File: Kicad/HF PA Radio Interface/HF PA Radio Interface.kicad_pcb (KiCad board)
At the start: 2 copper layers, 100 x 100 mm, 187 parts, among them J1 Conn_01x06, J10 Conn_01x03, J11 Conn_01x04, J12 Conn_01x02, J13 Conn_01x02, J14 Conn_01x02, J15 Conn_01x03, J16 Conn_01x04, J17 Conn_01x04, J18 Conn_01x04, J2 Conn_Coaxial, J3 Conn_Coaxial, J4 Conn_Coaxial, J5 Conn_01x05, J6 Conn_01x05, J7 Conn_01x04, J8 Conn_01x04, J9 Conn_01x04, K1 G2RL-1-E, Q1 BC848W, Q2 2N7002, Q3 DMG2305UX, U1 74LVC1G17, U10 74AHCT125, U2 74LVC74, U3 TLV9364, U4 ADS1015IDGS, U5 TLV9361, U6 MCP4728, U7 AP2204K-ADJ, U8 LTC1044, U9 74LVC1G17

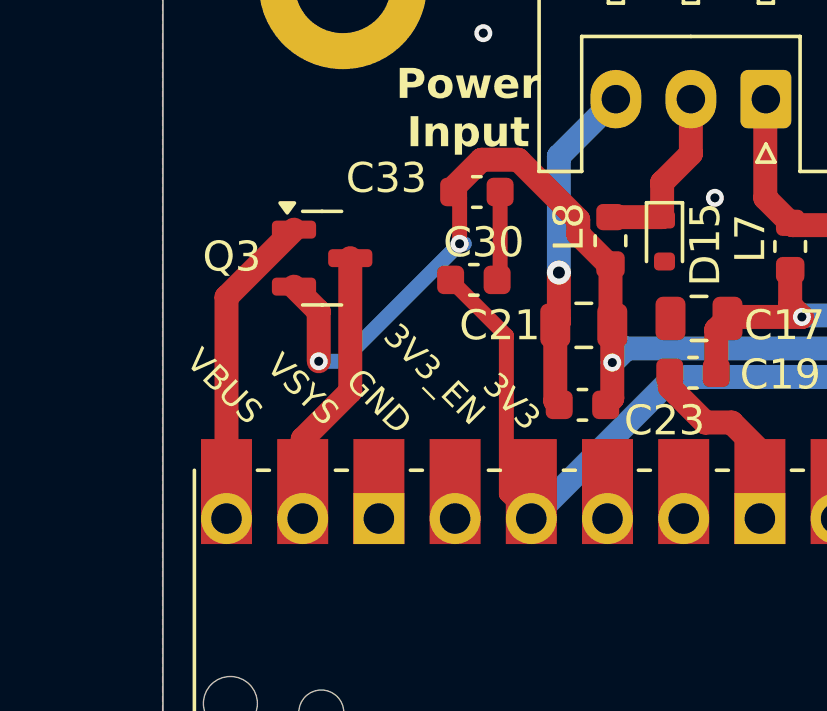
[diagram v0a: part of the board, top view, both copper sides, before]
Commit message: Updates to HF PA Interface and PA Power_V1
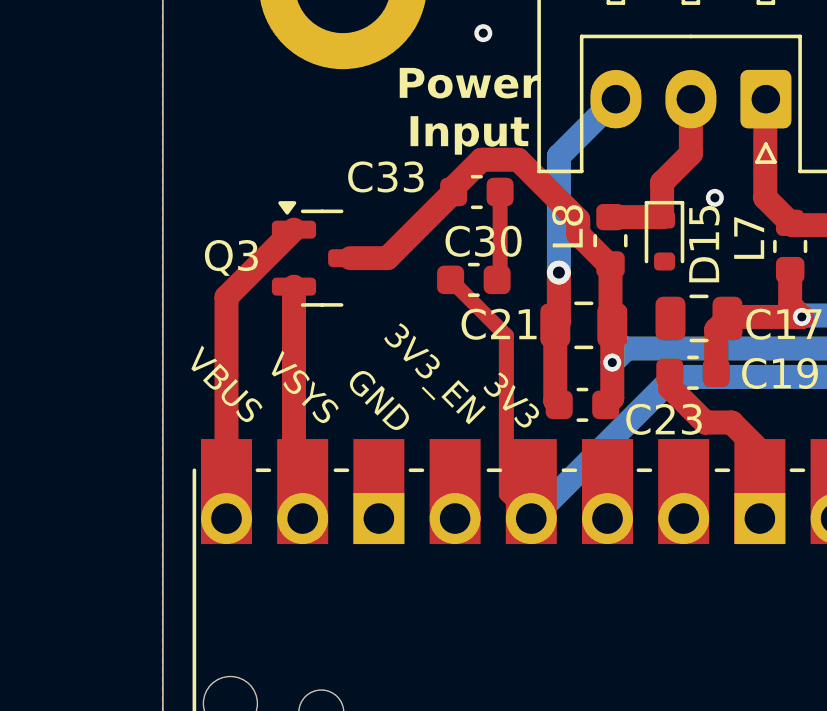
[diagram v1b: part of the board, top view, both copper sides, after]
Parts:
- C30, C33: value 10n -> 100n
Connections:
- Q3 pad 2: +5V -> Net-(A1-VSYS)
- Q3 pad 3: Net-(A1-VSYS) -> +5V
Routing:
- net +5V: track 130.6 -> 124.1 mm, vias 9 -> 7
- net Net-(A1-VSYS): track 9.36 -> 7.85 mm
